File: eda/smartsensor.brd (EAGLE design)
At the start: 33 x 27.9 mm, 43 parts, among them U1 ISL83491SOIC, U2 ATTINY1634, U3 3.3V

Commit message: Much tidying in pie.lbr
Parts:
- U2: device pie:SOIC20S -> pie:SOIC20
- moved U2 7.41 mm to (16.5, 14.9), turned to 180 degrees

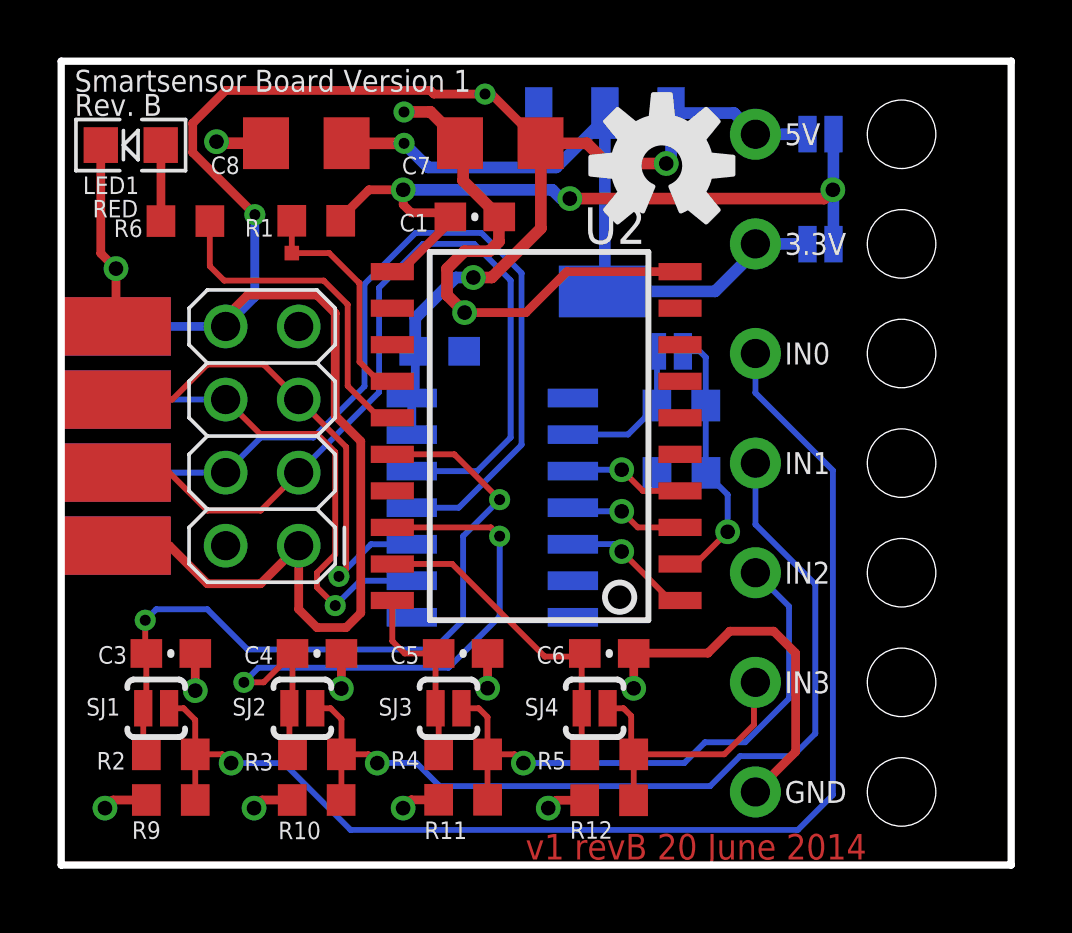
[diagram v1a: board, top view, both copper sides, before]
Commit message: Fixed ribboncable pinout
On battery_buzzer, smartsensor, smartsensor_Powered, team_flag, controller,
and grizzly_bear.
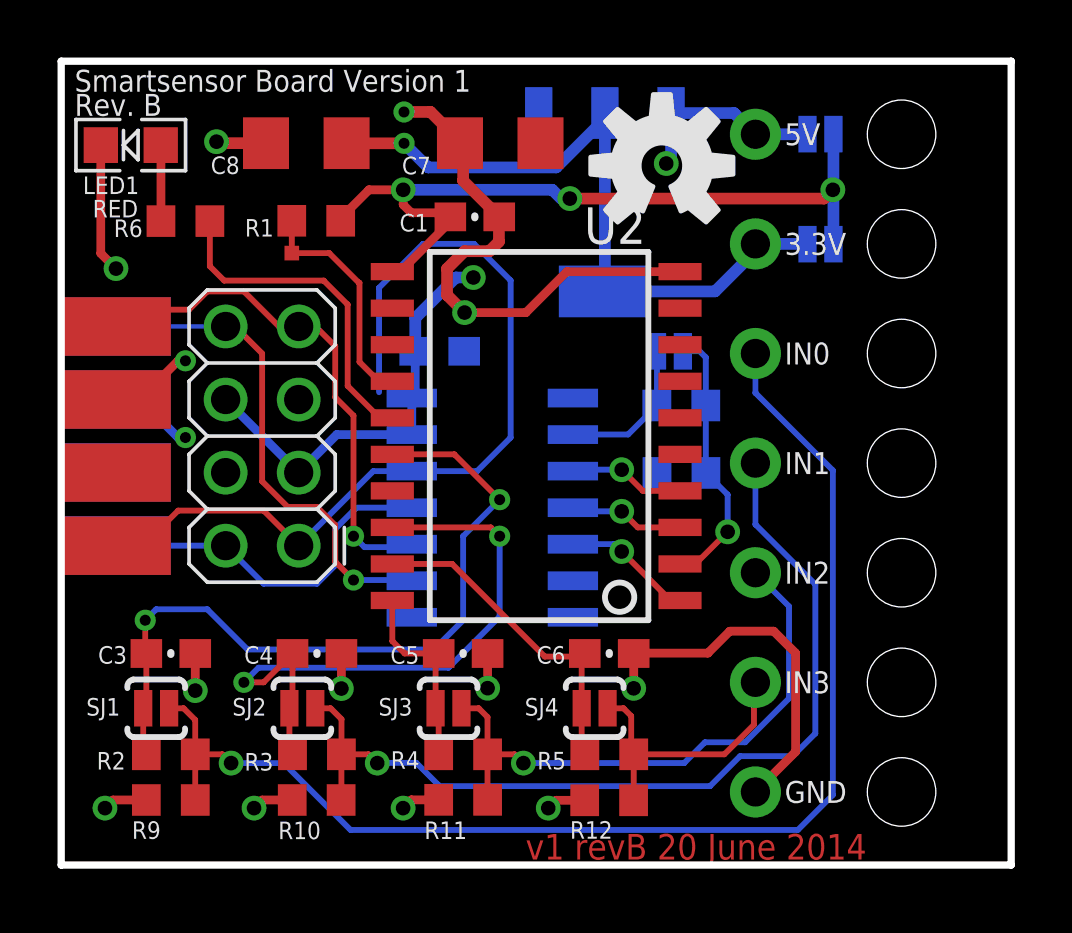
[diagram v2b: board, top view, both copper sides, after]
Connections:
- net 5V: now also U$7.3, U$7.6, U$8.3, U$8.6; no longer U$7.1, U$7.8, U$8.1, U$8.8
- net A_N: now also U$7.2, U$8.2; no longer U$7.4, U$8.4
- net A_P: now also U$7.1, U$8.1; no longer U$7.3, U$8.3
- net B_N: now also U$7.7, U$8.7; no longer U$7.5, U$8.5
- net B_P: now also U$7.8, U$8.8; no longer U$7.6, U$8.6
- net GND: now also U$7.4, U$7.5, U$8.4, U$8.5; no longer U$7.2, U$7.7, U$8.2, U$8.7
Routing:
- net 5V: track 77.6 -> 24.9 mm, vias 4 -> 3
- net A_N: track 30.9 -> 12.7 mm
- net GND: track 50.1 -> 51.1 mm, vias 12 -> 13
- net A_P: track 30.1 -> 31.1 mm
- net B_N: track 17.3 -> 18.0 mm
- added copper zone on layer 1, net 5V

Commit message: All jigs probe vias accessible after populating.
Also changed "VCC" signal name on jigs to "5V" to match boards.
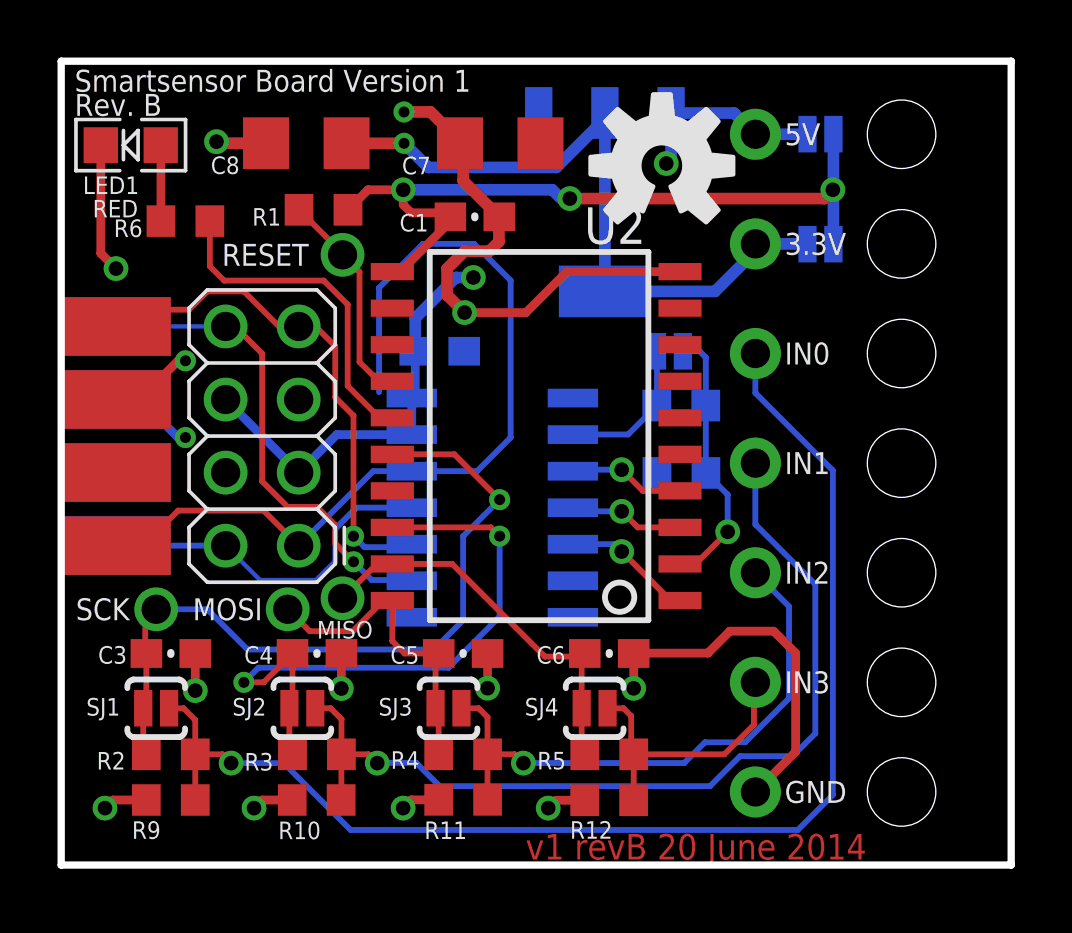
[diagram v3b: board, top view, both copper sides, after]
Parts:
- removed TP1: TEST-POINT2, pie:PAD.02X.02
- added MISO, MOSI, RESET, SCK: (no value), pie:POGO_PIN_394
- moved R1 0.46 mm to (9.12, 22.8)
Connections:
- net IO0: now also SCK.POGO_PIN
- net IO2: now also MOSI.POGO_PIN
- net IO3: now also MISO.POGO_PIN
- net RESET: now also RESET.POGO_PIN; no longer TP1.P$1
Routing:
- net IO2: track 6.81 -> 11.5 mm
- net IO3: track 11.5 -> 14.1 mm
- net IO0: vias 2 -> 1

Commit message: Added smartsensor variation checkboxes.
On smartsensor.brd and smartsensorPowered.brd.
Minor via shifting to accomodate text.
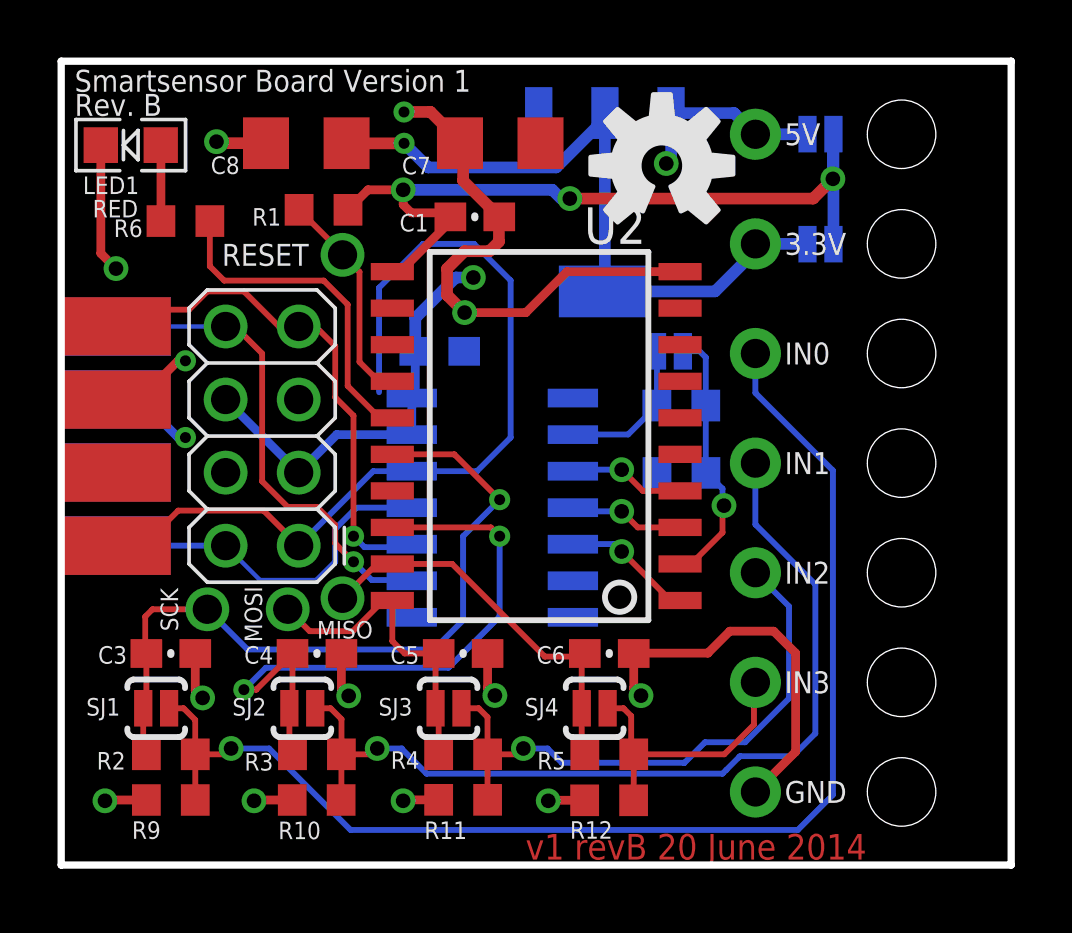
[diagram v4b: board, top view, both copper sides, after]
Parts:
- moved SCK 1.78 mm to (5.08, 8.89)
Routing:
- net GND: track 51.1 -> 52.2 mm
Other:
- board text added: "(c) Pioneers in Engineering. Design by: Vincent Donato and Devin He. This design is open source hardware. For more info, visit pioneers. berkeley.edu/ opensource"
- board text added: "A_IN"
- board text added: "A_OUT"
- board text added: "DEBUG"
- board text added: "D_I/O"
- board text added: "GRIZZLY"
- board text added: "I2C"
- board text added: "SENSOR VARIANT"
- board text added: "SPI"
- board text added: "UART"
- board text removed: "(c) Pioneers in Engineering Design by: Vincent Donato and Devin He This design is open source hardware. For more information, visit pioneers.berkeley.edu/opensource"

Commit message: Standardized copyright and "Design by" info among boards.
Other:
- board text added: "(c) Pioneers in Engineering. Design by: Vincent Donato and Devin He. This design is open source hardware. hardware. For more info, visit pioneers.berkeley.edu/opensource."
- board text removed: "(c) Pioneers in Engineering. Design by: Vincent Donato and Devin He. This design is open source hardware. For more info, visit pioneers. berkeley.edu/ opensource"
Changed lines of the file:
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@@
 <text x="6.35" y="2.54" size="1.27" layer="22" font="vector" ratio="15" rot="MR0">SPI</text>
 <rectangle x1="6.731" y1="2.54" x2="8.001" y2="3.81" layer="22"/>
-<text x="19.939" y="6.477" size="0.6096" layer="22" ratio="20" rot="MR90">(c) Pioneers in Engineering.  Design
-by: Vincent Donato and Devin He.
+<text x="25.019" y="0.635" size="0.762" layer="22" font="vector" ratio="20" rot="MR90">(c) Pioneers in Engineering.
+Design by:  Vincent Donato and Devin He.
 This design is open source hardware.
-For more info,
-visit pioneers.
-berkeley.edu/
-opensource</text>
+hardware.  For more info, visit
+pioneers.berkeley.edu/opensource.</text>
 <wire x1="0.381" y1="0.381" x2="21.844" y2="0.381" width="0.2032" layer="22"/>
 <wire x1="21.844" y1="0.381" x2="21.844" y2="5.969" width="0.2032" layer="22"/>
